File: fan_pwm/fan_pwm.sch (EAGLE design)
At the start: 17 parts, among them J1 PJ-058A, U1 LTC6992CS6-4TRMPBF, U2 SN74LVC1G34DBVR, U3 MIC5205-5.0YM5-TR

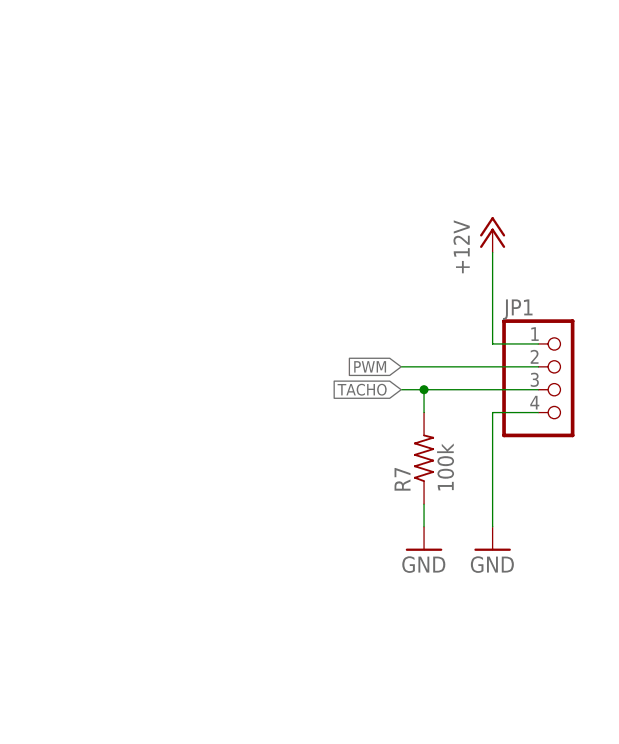
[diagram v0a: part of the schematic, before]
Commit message: tacho pullup
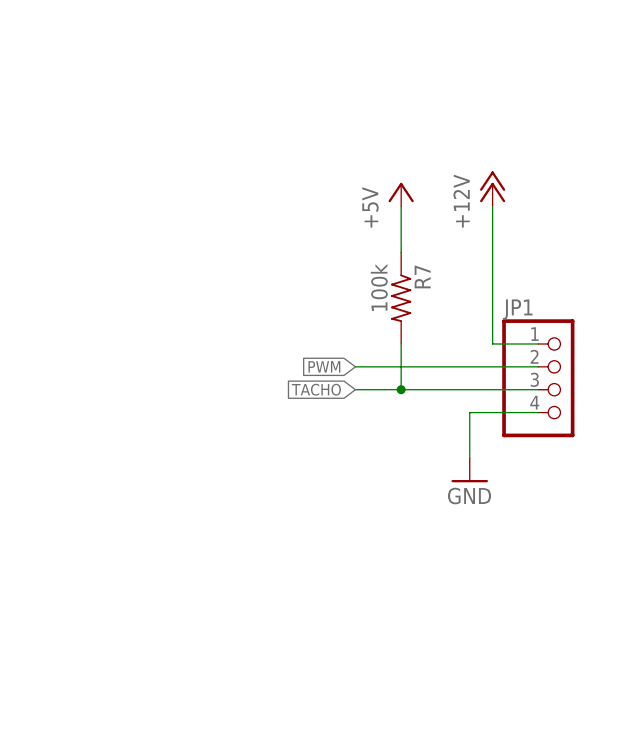
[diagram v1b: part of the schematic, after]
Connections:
- net +5V: now also R7.1
- net GND: no longer R7.1
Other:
- moved on the sheet: R7
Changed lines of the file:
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@@
 <part name="P+2" library="supply1" library_urn="urn:adsk.eagle:library:371" deviceset="+12V" device=""/>
 <part name="R7" library="rcl" library_urn="urn:adsk.eagle:library:334" deviceset="R-US_" device="R0805" package3d_urn="urn:adsk.eagle:package:23553/2" value="100k"/>
-<part name="GND6" library="supply1" library_urn="urn:adsk.eagle:library:371" deviceset="GND" device=""/>
 <part name="R4" library="P0915N-QC20BR5K" library_urn="urn:adsk.eagle:library:30572053" deviceset="P0915N-QC20BR5K" device="" package3d_urn="urn:adsk.eagle:package:30572056/3" value="P0915N-QC20BR[5K]"/>
 <part name="GND7" library="supply1" library_urn="urn:adsk.eagle:library:371" deviceset="GND" device=""/>
@@
 <part name="P+12" library="supply1" library_urn="urn:adsk.eagle:library:371" deviceset="+12V" device=""/>
 <part name="FRAME1" library="frames" library_urn="urn:adsk.eagle:library:229" deviceset="FRAME_A_L" device=""/>
+<part name="P+13" library="supply1" library_urn="urn:adsk.eagle:library:371" deviceset="+5V" device=""/>
 </parts>
 <sheets>
@@
 <attribute name="VALUE" x="252.73" y="99.06" size="1.778" layer="96"/>
 </instance>
-<instance part="GND5" gate="1" x="251.46" y="88.9" smashed="yes">
-<attribute name="VALUE" x="248.92" y="86.36" size="1.778" layer="96"/>
-</instance>
-<instance part="P+2" gate="1" x="251.46" y="124.46" smashed="yes">
-<attribute name="VALUE" x="248.92" y="119.38" size="1.778" layer="96" rot="R90"/>
-</instance>
-<instance part="R7" gate="G$1" x="243.84" y="99.06" smashed="yes" rot="R90">
-<attribute name="NAME" x="242.3414" y="95.25" size="1.778" layer="95" rot="R90"/>
-<attribute name="VALUE" x="247.142" y="95.25" size="1.778" layer="96" rot="R90"/>
-</instance>
-<instance part="GND6" gate="1" x="243.84" y="88.9" smashed="yes">
-<attribute name="VALUE" x="241.3" y="86.36" size="1.778" layer="96"/>
+<instance part="GND5" gate="1" x="248.92" y="96.52" smashed="yes">
+<attribute name="VALUE" x="246.38" y="93.98" size="1.778" layer="96"/>
+</instance>
+<instance part="P+2" gate="1" x="251.46" y="129.54" smashed="yes">
+<attribute name="VALUE" x="248.92" y="124.46" size="1.778" layer="96" rot="R90"/>
+</instance>
+<instance part="R7" gate="G$1" x="241.3" y="116.84" smashed="yes" rot="R270">
+<attribute name="NAME" x="242.7986" y="120.65" size="1.778" layer="95" rot="R270"/>
+<attribute name="VALUE" x="237.998" y="120.65" size="1.778" layer="96" rot="R270"/>
 </instance>
 <instance part="R4" gate="G$1" x="152.4" y="175.26" smashed="yes">
@@
 <attribute name="DRAWING_NAME" x="190.5" y="19.05" size="2.54" layer="94"/>
 </instance>
+<instance part="P+13" gate="1" x="241.3" y="129.54" smashed="yes">
+<attribute name="VALUE" x="238.76" y="124.46" size="1.778" layer="96" rot="R90"/>
+</instance>
 </instances>
 <busses>
@@
 <segment>
 <pinref part="JP1" gate="A" pin="4"/>
-<wire x1="256.54" y1="104.14" x2="251.46" y2="104.14" width="0.1524" layer="91"/>
-<wire x1="251.46" y1="104.14" x2="251.46" y2="91.44" width="0.1524" layer="91"/>
+<wire x1="256.54" y1="104.14" x2="248.92" y2="104.14" width="0.1524" layer="91"/>
+<wire x1="248.92" y1="104.14" x2="248.92" y2="99.06" width="0.1524" layer="91"/>
 <pinref part="GND5" gate="1" pin="GND"/>
-</segment>
-<segment>
-<pinref part="R7" gate="G$1" pin="1"/>
-<pinref part="GND6" gate="1" pin="GND"/>
-<wire x1="243.84" y1="93.98" x2="243.84" y2="91.44" width="0.1524" layer="91"/>
 </segment>
 <segment>
@@
 <wire x1="106.68" y1="27.94" x2="106.68" y2="35.56" width="0.1524" layer="91"/>
 </segment>
+<segment>
+<pinref part="R7" gate="G$1" pin="1"/>
+<pinref part="P+13" gate="1" pin="+5V"/>
+<wire x1="241.3" y1="121.92" x2="241.3" y2="127" width="0.1524" layer="91"/>
+</segment>
 </net>
 <net name="PWM" class="0">
 <segment>
 <pinref part="JP1" gate="A" pin="2"/>
-<wire x1="256.54" y1="109.22" x2="241.3" y2="109.22" width="0.1524" layer="91"/>
-<label x="241.3" y="109.22" size="1.27" layer="95" rot="R180" xref="yes"/>
+<wire x1="256.54" y1="109.22" x2="236.22" y2="109.22" width="0.1524" layer="91"/>
+<label x="236.22" y="109.22" size="1.27" layer="95" rot="R180" xref="yes"/>
 </segment>
 <segment>
@@
 <segment>
 <pinref part="JP1" gate="A" pin="3"/>
-<wire x1="256.54" y1="106.68" x2="243.84" y2="106.68" width="0.1524" layer="91"/>
-<label x="241.3" y="106.68" size="1.27" layer="95" rot="R180" xref="yes"/>
+<wire x1="256.54" y1="106.68" x2="241.3" y2="106.68" width="0.1524" layer="91"/>
+<label x="236.22" y="106.68" size="1.27" layer="95" rot="R180" xref="yes"/>
 <pinref part="R7" gate="G$1" pin="2"/>
-<wire x1="243.84" y1="106.68" x2="241.3" y2="106.68" width="0.1524" layer="91"/>
-<wire x1="243.84" y1="104.14" x2="243.84" y2="106.68" width="0.1524" layer="91"/>
-<junction x="243.84" y="106.68"/>
+<wire x1="241.3" y1="106.68" x2="236.22" y2="106.68" width="0.1524" layer="91"/>
+<wire x1="241.3" y1="111.76" x2="241.3" y2="106.68" width="0.1524" layer="91"/>
+<junction x="241.3" y="106.68"/>
 </segment>
 </net>
@@
 <pinref part="JP1" gate="A" pin="1"/>
 <wire x1="256.54" y1="111.76" x2="251.46" y2="111.76" width="0.1524" layer="91"/>
-<wire x1="251.46" y1="111.76" x2="251.46" y2="121.92" width="0.1524" layer="91"/>
+<wire x1="251.46" y1="111.76" x2="251.46" y2="127" width="0.1524" layer="91"/>
 <pinref part="P+2" gate="1" pin="+12V"/>
 </segment>
